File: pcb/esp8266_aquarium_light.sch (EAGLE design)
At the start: 19 parts, among them Q1 BUZ11, Q2 BUZ11, Q3 BUZ11, Q4 BUZ11, T1 BC337, T2 BC337, T3 BC337, T4 BC337

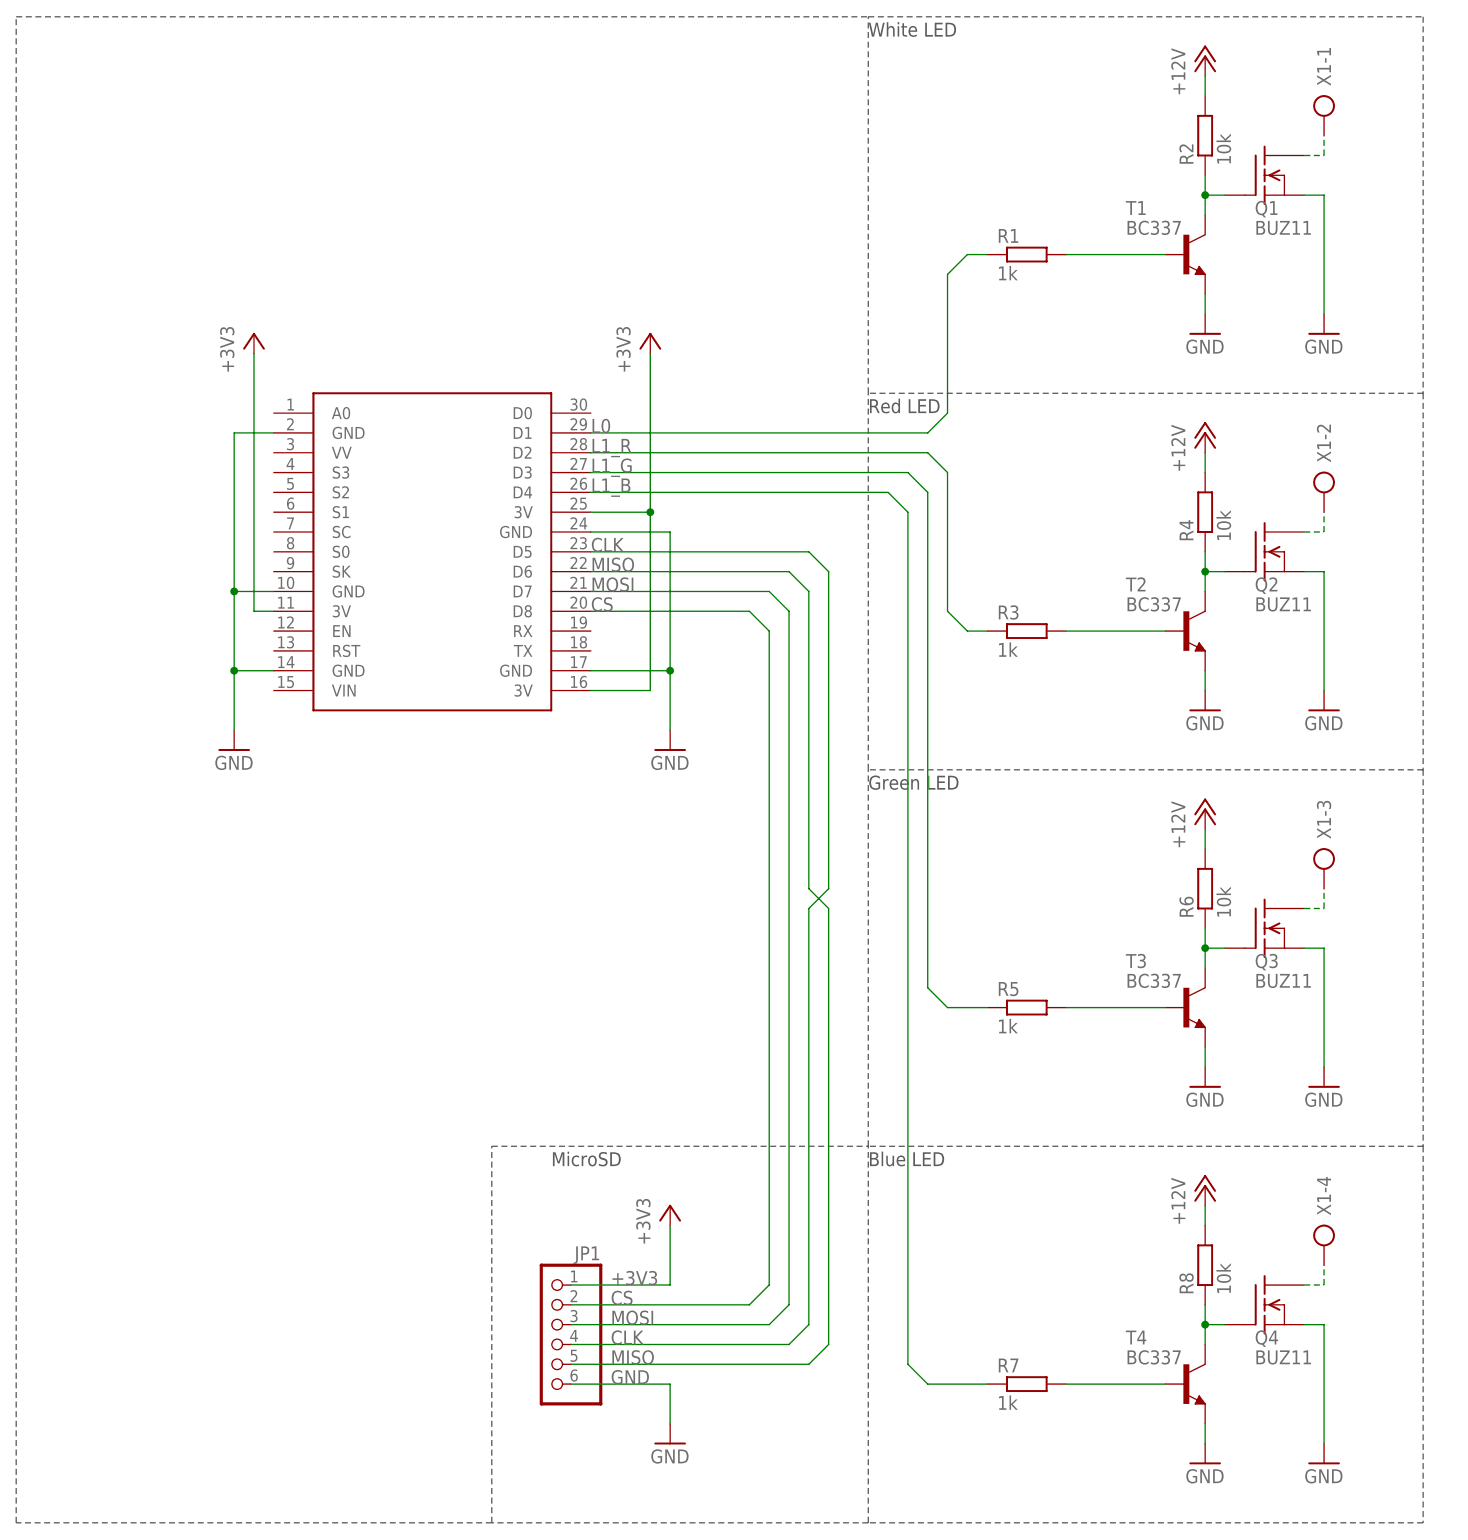
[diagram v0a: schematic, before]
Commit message: UI updated: -vue.js used -tabs added: day mode/night mode/settings Firmware - refactoring
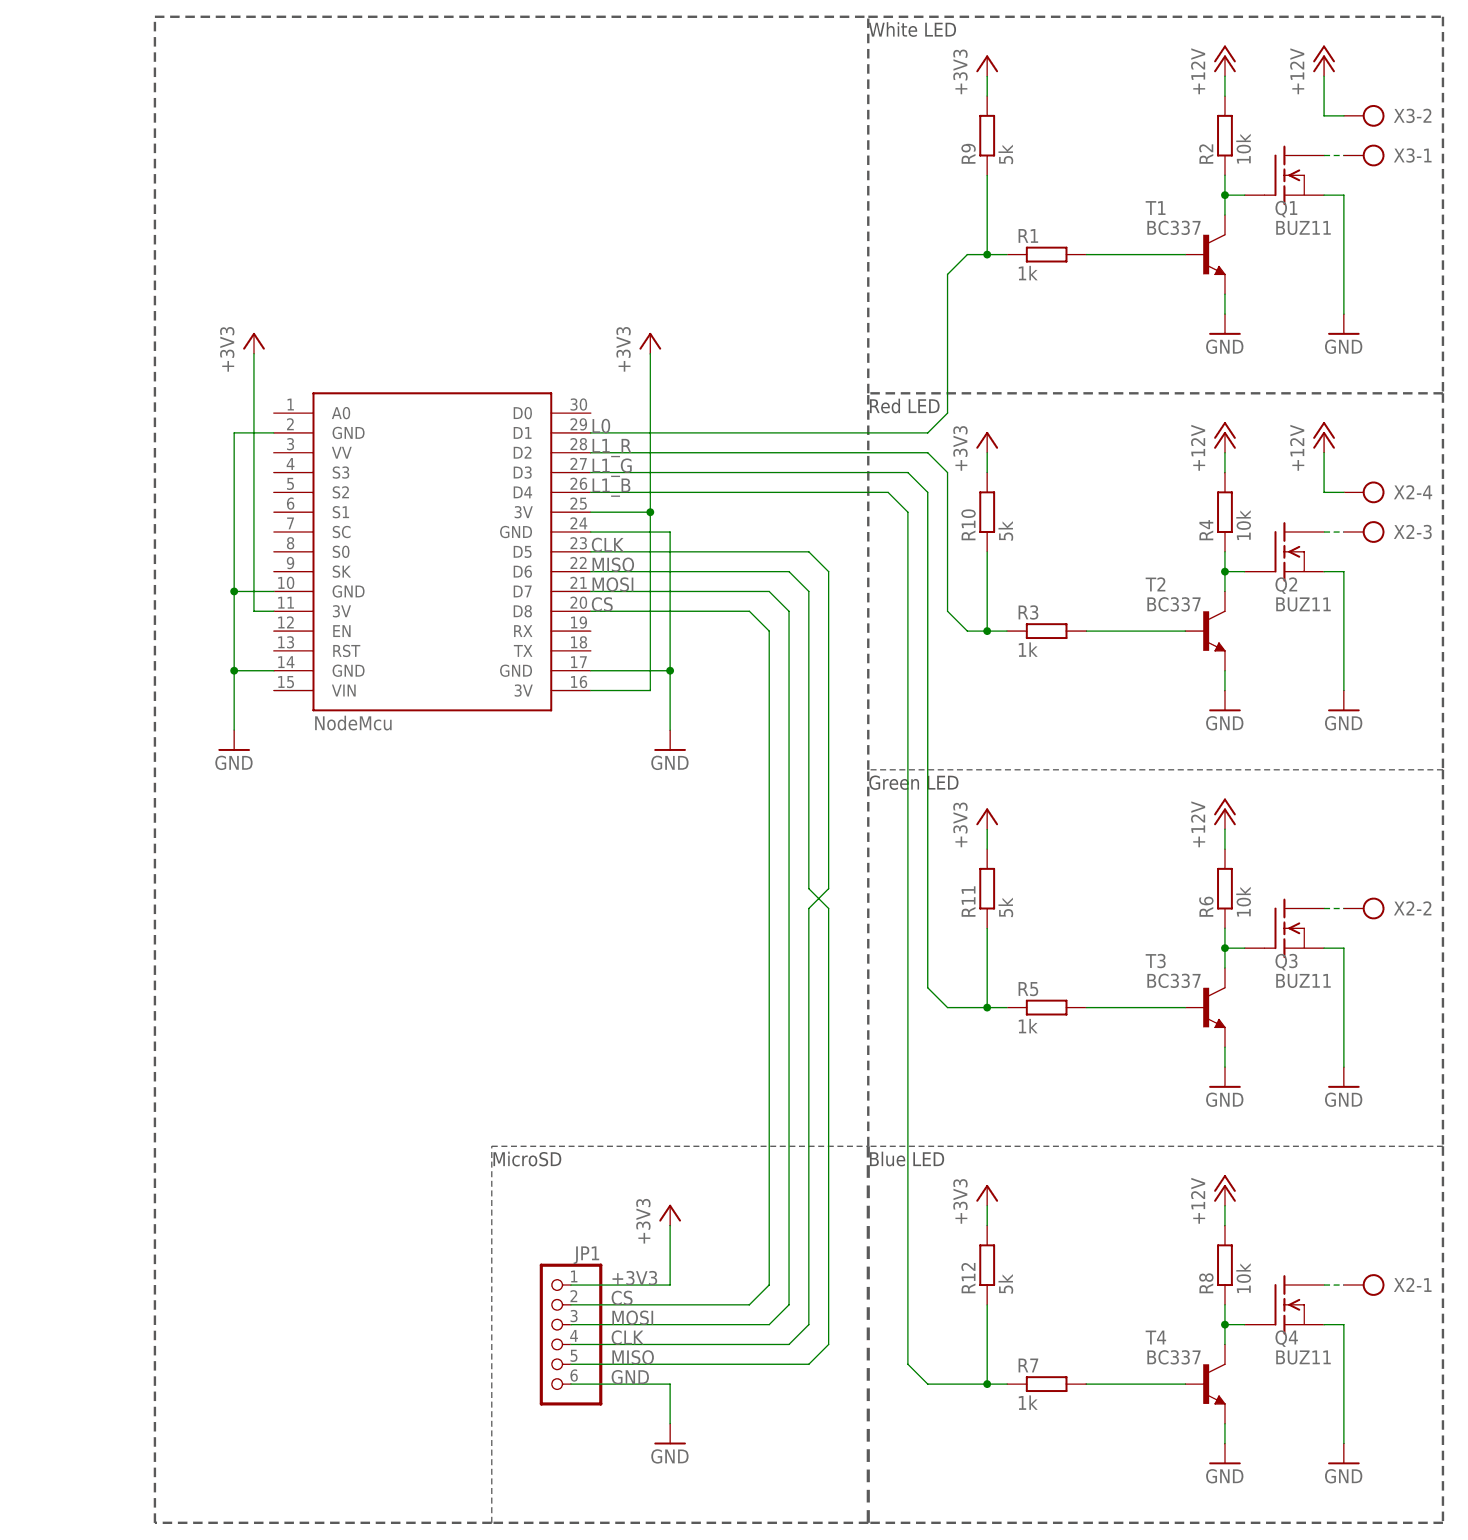
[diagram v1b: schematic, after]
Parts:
- removed X1: (no value), con-ptr500:AK500/4
- added R10, R11, R12, R9: 5k, resistor:R-EU_0309/12
- added X2: (no value), con-ptr500:AK500/4
- added X3: (no value), con-ptr500:AK500/2
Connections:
- net +12V: now also X2-4.KL, X3-2.KL
- net +3V3: now also R10.2, R11.2, R12.2, R9.2
- net L0: now also R9.1
- net L1_B: now also R12.1
- net L1_G: now also R11.1
- net L1_R: now also R10.1
- net N$10: now also X3-1.KL; no longer X1-1.KL
- net N$11: now also X2-2.KL; no longer X1-3.KL
- net N$12: now also X2-1.KL; no longer X1-4.KL
- net N$9: now also X2-3.KL; no longer X1-2.KL
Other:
- note added: "NodeMcu"
- moved on the sheet: Q1, Q2, Q3, Q4, R1, R2, R3, R4, R5, R6, R7, R8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
